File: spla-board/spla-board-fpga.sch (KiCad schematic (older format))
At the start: 32 parts, among them J2 J_JTAG, U1 LFE5U-45F-BG256

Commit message: schematic: Add Digikey and ManufacturerId fields to big components.
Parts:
- U1: Digikey (none) -> 220-2198-ND; Manufacturer Id (none) -> LFE4U-45F-6BG256C
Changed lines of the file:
@@
 F 2 "Package_BGA:BGA-256_14.0x14.0mm_Layout16x16_P0.8mm_Ball0.45mm_Pad0.32mm_NSMD" H 3050 4850 39  0001 C CNN
 F 3 "" H 3050 4850 39  0001 C CNN
+F 4 "220-2198-ND" H 4000 2850 50  0001 C CNN "Digikey"
+F 5 "LFE4U-45F-6BG256C" H 4000 2850 50  0001 C CNN "Manufacturer Id"
 	2    4000 2850
 	1    0    0    -1
@@
 F 2 "Package_BGA:BGA-256_14.0x14.0mm_Layout16x16_P0.8mm_Ball0.45mm_Pad0.32mm_NSMD" H 5550 4850 39  0001 C CNN
 F 3 "" H 5550 4850 39  0001 C CNN
+F 4 "220-2198-ND" H 6500 2850 50  0001 C CNN "Digikey"
+F 5 "LFE4U-45F-6BG256C" H 6500 2850 50  0001 C CNN "Manufacturer Id"
 	3    6500 2850
 	1    0    0    -1
@@
 F 2 "Package_BGA:BGA-256_14.0x14.0mm_Layout16x16_P0.8mm_Ball0.45mm_Pad0.32mm_NSMD" H 8050 4850 39  0001 C CNN
 F 3 "" H 8050 4850 39  0001 C CNN
+F 4 "220-2198-ND" H 9000 2850 50  0001 C CNN "Digikey"
+F 5 "LFE4U-45F-6BG256C" H 9000 2850 50  0001 C CNN "Manufacturer Id"
 	4    9000 2850
 	1    0    0    -1
@@
 F 2 "Package_BGA:BGA-256_14.0x14.0mm_Layout16x16_P0.8mm_Ball0.45mm_Pad0.32mm_NSMD" H 900 12100 39  0001 C CNN
 F 3 "" H 900 12100 39  0001 C CNN
+F 4 "220-2198-ND" H 1850 10100 50  0001 C CNN "Digikey"
+F 5 "LFE4U-45F-6BG256C" H 1850 10100 50  0001 C CNN "Manufacturer Id"
 	8    1850 10100
 	1    0    0    -1
@@
 F 2 "Package_BGA:BGA-256_14.0x14.0mm_Layout16x16_P0.8mm_Ball0.45mm_Pad0.32mm_NSMD" H 7900 12050 39  0001 C CNN
 F 3 "" H 7900 12050 39  0001 C CNN
+F 4 "220-2198-ND" H 8850 10050 50  0001 C CNN "Digikey"
+F 5 "LFE4U-45F-6BG256C" H 8850 10050 50  0001 C CNN "Manufacturer Id"
 	9    8850 10050
 	1    0    0    -1
@@
 F 2 "Package_BGA:BGA-256_14.0x14.0mm_Layout16x16_P0.8mm_Ball0.45mm_Pad0.32mm_NSMD" H 10550 4850 39  0001 C CNN
 F 3 "" H 10550 4850 39  0001 C CNN
+F 4 "220-2198-ND" H 11500 2850 50  0001 C CNN "Digikey"
+F 5 "LFE4U-45F-6BG256C" H 11500 2850 50  0001 C CNN "Manufacturer Id"
 	5    11500 2850
 	1    0    0    -1
@@
 F 2 "Package_BGA:BGA-256_14.0x14.0mm_Layout16x16_P0.8mm_Ball0.45mm_Pad0.32mm_NSMD" H 1500 9850 39  0001 C CNN
 F 3 "" H 1500 9850 39  0001 C CNN
+F 4 "220-2198-ND" H 2450 7850 50  0001 C CNN "Digikey"
+F 5 "LFE4U-45F-6BG256C" H 2450 7850 50  0001 C CNN "Manufacturer Id"
 	7    2450 7850
 	1    0    0    -1
@@
 F 2 "Package_BGA:BGA-256_14.0x14.0mm_Layout16x16_P0.8mm_Ball0.45mm_Pad0.32mm_NSMD" H 550 5250 39  0001 C CNN
 F 3 "" H 550 5250 39  0001 C CNN
+F 4 "220-2198-ND" H 1500 3250 50  0001 C CNN "Digikey"
+F 5 "LFE4U-45F-6BG256C" H 1500 3250 50  0001 C CNN "Manufacturer Id"
 	1    1500 3250
 	1    0    0    -1
@@
 F 2 "Package_BGA:BGA-256_14.0x14.0mm_Layout16x16_P0.8mm_Ball0.45mm_Pad0.32mm_NSMD" H 13050 4850 39  0001 C CNN
 F 3 "" H 13050 4850 39  0001 C CNN
+F 4 "220-2198-ND" H 14000 2850 50  0001 C CNN "Digikey"
+F 5 "LFE4U-45F-6BG256C" H 14000 2850 50  0001 C CNN "Manufacturer Id"
 	6    14000 2850
 	1    0    0    -1

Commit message: schematic: Select LED part.
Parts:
- D5, D6, D7, D8: Digikey (none) -> 732-4986-1-ND; Manufacturer Id (none) -> 150080VS75000
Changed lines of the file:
@@
 F 2 "LED_SMD:LED_0805_2012Metric" H 5550 9750 50  0001 C CNN
 F 3 "~" H 5550 9750 50  0001 C CNN
+F 4 "732-4986-1-ND" H 5550 9750 50  0001 C CNN "Digikey"
+F 5 "150080VS75000" H 5550 9750 50  0001 C CNN "Manufacturer Id"
 	1    5550 9750
 	0    -1   -1   0
@@
 F 2 "LED_SMD:LED_0805_2012Metric" H 5950 9750 50  0001 C CNN
 F 3 "~" H 5950 9750 50  0001 C CNN
+F 4 "732-4986-1-ND" H 5950 9750 50  0001 C CNN "Digikey"
+F 5 "150080VS75000" H 5950 9750 50  0001 C CNN "Manufacturer Id"
 	1    5950 9750
 	0    -1   -1   0
@@
 F 2 "LED_SMD:LED_0805_2012Metric" H 4750 9750 50  0001 C CNN
 F 3 "~" H 4750 9750 50  0001 C CNN
+F 4 "732-4986-1-ND" H 4750 9750 50  0001 C CNN "Digikey"
+F 5 "150080VS75000" H 4750 9750 50  0001 C CNN "Manufacturer Id"
 	1    4750 9750
 	0    -1   -1   0
@@
 F 2 "LED_SMD:LED_0805_2012Metric" H 5150 9750 50  0001 C CNN
 F 3 "~" H 5150 9750 50  0001 C CNN
+F 4 "732-4986-1-ND" H 5150 9750 50  0001 C CNN "Digikey"
+F 5 "150080VS75000" H 5150 9750 50  0001 C CNN "Manufacturer Id"
 	1    5150 9750
 	0    -1   -1   0

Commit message: schematic: Add part numbers for pinheaders (albeit that these are breakaways, and it's not one-per-part).
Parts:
- J2: Digikey (none) -> S1011EC-40-ND; Manufacturer Id (none) -> PRPC040SAAN-RC
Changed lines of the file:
@@
 F 2 "Connector_PinHeader_2.54mm:PinHeader_1x04_P2.54mm_Vertical" H 2700 9650 50  0001 C CNN
 F 3 "~" H 2700 9650 50  0001 C CNN
+F 4 "S1011EC-40-ND" H 2700 9650 50  0001 C CNN "Digikey"
+F 5 "PRPC040SAAN-RC" H 2700 9650 50  0001 C CNN "Manufacturer Id"
 	1    2700 9650
 	0    -1   -1   0

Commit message: schematic/pcb: Add test points for remaining three FPGA pins.
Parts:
- added TP7, TP8, TP9: TestPoint, TestPoint:TestPoint_Pad_D2.0mm, symbol Connector:TestPoint
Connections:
- net FPGA_EXTRA1: now reaches U1.C1 (PL14A)
- net FPGA_EXTRA1: now also TP7.1
- net FPGA_EXTRA2: now reaches U1.D1 (PL17A)
- net FPGA_EXTRA2: now also TP8.1
- net FPGA_EXTRA3: now reaches U1.E3 (PL14C)
- net FPGA_EXTRA3: now also TP9.1
- no-connect marks 21 -> 18
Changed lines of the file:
@@
 NoConn ~ 14650 3600
 NoConn ~ 14650 2500
-NoConn ~ 14650 1700
-NoConn ~ 14650 1900
-NoConn ~ 14650 2100
 NoConn ~ 7150 3600
 NoConn ~ 7150 3300
@@
 Text Notes 7950 7350 0    50   ~ 0
 Note: by above logic, 3.3V is short 9x 0.01uF decoupling capacitors, due to lack of space.
+Text GLabel 14650 1700 2    50   Output ~ 0
+FPGA_EXTRA1
+Text GLabel 14650 2100 2    50   Output ~ 0
+FPGA_EXTRA2
+Text GLabel 14650 1900 2    50   Output ~ 0
+FPGA_EXTRA3
+Text GLabel 14800 5300 2    50   Output ~ 0
+FPGA_EXTRA1
+Text GLabel 14800 5700 2    50   Output ~ 0
+FPGA_EXTRA2
+Text GLabel 14800 6100 2    50   Output ~ 0
+FPGA_EXTRA3
+$Comp
+L Connector:TestPoint TP7
+U 1 1 5EA65145
+P 14700 5200
+F 0 "TP7" H 14758 5318 50  0000 L CNN
+F 1 "TestPoint" H 14758 5227 50  0000 L CNN
+F 2 "TestPoint:TestPoint_Pad_D2.0mm" H 14900 5200 50  0001 C CNN
+F 3 "~" H 14900 5200 50  0001 C CNN
+	1    14700 5200
+	1    0    0    -1
+$EndComp
+$Comp
+L Connector:TestPoint TP8
+U 1 1 5EA6567A
+P 14700 5600
+F 0 "TP8" H 14758 5718 50  0000 L CNN
+F 1 "TestPoint" H 14758 5627 50  0000 L CNN
+F 2 "TestPoint:TestPoint_Pad_D2.0mm" H 14900 5600 50  0001 C CNN
+F 3 "~" H 14900 5600 50  0001 C CNN
+	1    14700 5600
+	1    0    0    -1
+$EndComp
+$Comp
+L Connector:TestPoint TP9
+U 1 1 5EA6C737
+P 14700 6000
+F 0 "TP9" H 14758 6118 50  0000 L CNN
+F 1 "TestPoint" H 14758 6027 50  0000 L CNN
+F 2 "TestPoint:TestPoint_Pad_D2.0mm" H 14900 6000 50  0001 C CNN
+F 3 "~" H 14900 6000 50  0001 C CNN
+	1    14700 6000
+	1    0    0    -1
+$EndComp
+Wire Wire Line
+	14800 5300 14700 5300
+Wire Wire Line
+	14700 5300 14700 5200
+Wire Wire Line
+	14800 5700 14700 5700
+Wire Wire Line
+	14700 5700 14700 5600
+Wire Wire Line
+	14800 6100 14700 6100
+Wire Wire Line
+	14700 6100 14700 6000
 $EndSCHEMATC

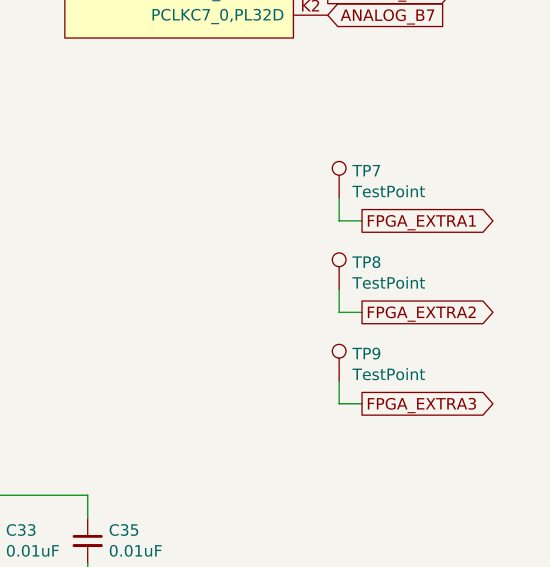
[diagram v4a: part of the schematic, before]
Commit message: schematic/pcb: Add BoM-only symbols.
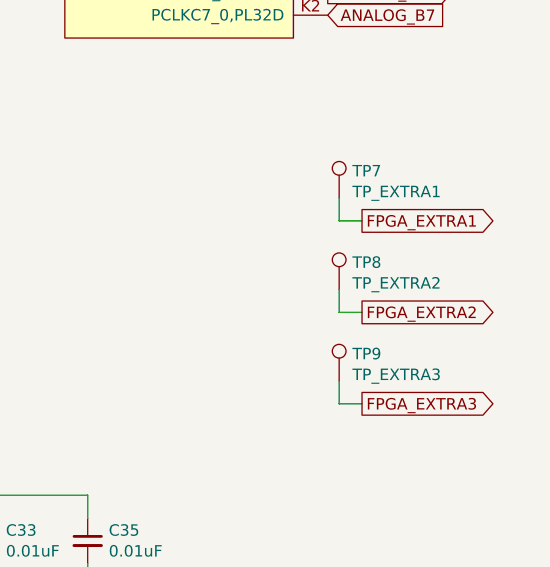
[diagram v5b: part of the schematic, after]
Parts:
- TP7: value TestPoint -> TP_EXTRA1; Digikey (none) -> N/A; Manufacturer Id (none) -> N/A
- TP8: value TestPoint -> TP_EXTRA2; Digikey (none) -> N/A; Manufacturer Id (none) -> N/A
- TP9: value TestPoint -> TP_EXTRA3; Digikey (none) -> N/A; Manufacturer Id (none) -> N/A
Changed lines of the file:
@@
 P 14700 5200
 F 0 "TP7" H 14758 5318 50  0000 L CNN
-F 1 "TestPoint" H 14758 5227 50  0000 L CNN
+F 1 "TP_EXTRA1" H 14758 5227 50  0000 L CNN
 F 2 "TestPoint:TestPoint_Pad_D2.0mm" H 14900 5200 50  0001 C CNN
 F 3 "~" H 14900 5200 50  0001 C CNN
+F 4 "N/A" H 14700 5200 50  0001 C CNN "Digikey"
+F 5 "N/A" H 14700 5200 50  0001 C CNN "Manufacturer Id"
 	1    14700 5200
 	1    0    0    -1
@@
 P 14700 5600
 F 0 "TP8" H 14758 5718 50  0000 L CNN
-F 1 "TestPoint" H 14758 5627 50  0000 L CNN
+F 1 "TP_EXTRA2" H 14758 5627 50  0000 L CNN
 F 2 "TestPoint:TestPoint_Pad_D2.0mm" H 14900 5600 50  0001 C CNN
 F 3 "~" H 14900 5600 50  0001 C CNN
+F 4 "N/A" H 14700 5600 50  0001 C CNN "Digikey"
+F 5 "N/A" H 14700 5600 50  0001 C CNN "Manufacturer Id"
 	1    14700 5600
 	1    0    0    -1
@@
 P 14700 6000
 F 0 "TP9" H 14758 6118 50  0000 L CNN
-F 1 "TestPoint" H 14758 6027 50  0000 L CNN
+F 1 "TP_EXTRA3" H 14758 6027 50  0000 L CNN
 F 2 "TestPoint:TestPoint_Pad_D2.0mm" H 14900 6000 50  0001 C CNN
 F 3 "~" H 14900 6000 50  0001 C CNN
+F 4 "N/A" H 14700 6000 50  0001 C CNN "Digikey"
+F 5 "N/A" H 14700 6000 50  0001 C CNN "Manufacturer Id"
 	1    14700 6000
 	1    0    0    -1

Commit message: bom: Add manufacturers.
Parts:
- D5, D6, D7, D8: Manufacturer (none) -> Wuerth Electronik
- J2: Manufacturer (none) -> Sullins Connector Solutions
- TP7, TP8, TP9: Manufacturer (none) -> N/A
- U1: Manufacturer (none) -> Lattice Semiconductor Corporation
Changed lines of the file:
@@
 F 4 "220-2198-ND" H 4000 2850 50  0001 C CNN "Digikey"
 F 5 "LFE4U-45F-6BG256C" H 4000 2850 50  0001 C CNN "Manufacturer Id"
+F 6 "Lattice Semiconductor Corporation" H 4000 2850 50  0001 C CNN "Manufacturer"
 	2    4000 2850
 	1    0    0    -1
@@
 F 4 "220-2198-ND" H 6500 2850 50  0001 C CNN "Digikey"
 F 5 "LFE4U-45F-6BG256C" H 6500 2850 50  0001 C CNN "Manufacturer Id"
+F 6 "Lattice Semiconductor Corporation" H 6500 2850 50  0001 C CNN "Manufacturer"
 	3    6500 2850
 	1    0    0    -1
@@
 F 4 "220-2198-ND" H 9000 2850 50  0001 C CNN "Digikey"
 F 5 "LFE4U-45F-6BG256C" H 9000 2850 50  0001 C CNN "Manufacturer Id"
+F 6 "Lattice Semiconductor Corporation" H 9000 2850 50  0001 C CNN "Manufacturer"
 	4    9000 2850
 	1    0    0    -1
@@
 F 4 "220-2198-ND" H 1850 10100 50  0001 C CNN "Digikey"
 F 5 "LFE4U-45F-6BG256C" H 1850 10100 50  0001 C CNN "Manufacturer Id"
+F 6 "Lattice Semiconductor Corporation" H 1850 10100 50  0001 C CNN "Manufacturer"
 	8    1850 10100
 	1    0    0    -1
@@
 F 4 "220-2198-ND" H 8850 10050 50  0001 C CNN "Digikey"
 F 5 "LFE4U-45F-6BG256C" H 8850 10050 50  0001 C CNN "Manufacturer Id"
+F 6 "Lattice Semiconductor Corporation" H 8850 10050 50  0001 C CNN "Manufacturer"
 	9    8850 10050
 	1    0    0    -1
@@
 F 4 "220-2198-ND" H 11500 2850 50  0001 C CNN "Digikey"
 F 5 "LFE4U-45F-6BG256C" H 11500 2850 50  0001 C CNN "Manufacturer Id"
+F 6 "Lattice Semiconductor Corporation" H 11500 2850 50  0001 C CNN "Manufacturer"
 	5    11500 2850
 	1    0    0    -1
@@
 F 4 "S1011EC-40-ND" H 2700 9650 50  0001 C CNN "Digikey"
 F 5 "PRPC040SAAN-RC" H 2700 9650 50  0001 C CNN "Manufacturer Id"
+F 6 "Sullins Connector Solutions" H 2700 9650 50  0001 C CNN "Manufacturer"
 	1    2700 9650
 	0    -1   -1   0
@@
 F 4 "220-2198-ND" H 2450 7850 50  0001 C CNN "Digikey"
 F 5 "LFE4U-45F-6BG256C" H 2450 7850 50  0001 C CNN "Manufacturer Id"
+F 6 "Lattice Semiconductor Corporation" H 2450 7850 50  0001 C CNN "Manufacturer"
 	7    2450 7850
 	1    0    0    -1
@@
 F 4 "220-2198-ND" H 1500 3250 50  0001 C CNN "Digikey"
 F 5 "LFE4U-45F-6BG256C" H 1500 3250 50  0001 C CNN "Manufacturer Id"
+F 6 "Lattice Semiconductor Corporation" H 1500 3250 50  0001 C CNN "Manufacturer"
 	1    1500 3250
 	1    0    0    -1
@@
 F 4 "220-2198-ND" H 14000 2850 50  0001 C CNN "Digikey"
 F 5 "LFE4U-45F-6BG256C" H 14000 2850 50  0001 C CNN "Manufacturer Id"
+F 6 "Lattice Semiconductor Corporation" H 14000 2850 50  0001 C CNN "Manufacturer"
 	6    14000 2850
 	1    0    0    -1
@@
 F 4 "732-4986-1-ND" H 5550 9750 50  0001 C CNN "Digikey"
 F 5 "150080VS75000" H 5550 9750 50  0001 C CNN "Manufacturer Id"
+F 6 "Wuerth Electronik" H 5550 9750 50  0001 C CNN "Manufacturer"
 	1    5550 9750
 	0    -1   -1   0
@@
 F 4 "732-4986-1-ND" H 5950 9750 50  0001 C CNN "Digikey"
 F 5 "150080VS75000" H 5950 9750 50  0001 C CNN "Manufacturer Id"
+F 6 "Wuerth Electronik" H 5950 9750 50  0001 C CNN "Manufacturer"
 	1    5950 9750
 	0    -1   -1   0
@@
 F 4 "732-4986-1-ND" H 4750 9750 50  0001 C CNN "Digikey"
 F 5 "150080VS75000" H 4750 9750 50  0001 C CNN "Manufacturer Id"
+F 6 "Wuerth Electronik" H 4750 9750 50  0001 C CNN "Manufacturer"
 	1    4750 9750
 	0    -1   -1   0
@@
 F 4 "732-4986-1-ND" H 5150 9750 50  0001 C CNN "Digikey"
 F 5 "150080VS75000" H 5150 9750 50  0001 C CNN "Manufacturer Id"
+F 6 "Wuerth Electronik" H 5150 9750 50  0001 C CNN "Manufacturer"
 	1    5150 9750
 	0    -1   -1   0
@@
 F 4 "N/A" H 14700 5200 50  0001 C CNN "Digikey"
 F 5 "N/A" H 14700 5200 50  0001 C CNN "Manufacturer Id"
+F 6 "N/A" H 14700 5200 50  0001 C CNN "Manufacturer"
 	1    14700 5200
 	1    0    0    -1
@@
 F 4 "N/A" H 14700 5600 50  0001 C CNN "Digikey"
 F 5 "N/A" H 14700 5600 50  0001 C CNN "Manufacturer Id"
+F 6 "N/A" H 14700 5600 50  0001 C CNN "Manufacturer"
 	1    14700 5600
 	1    0    0    -1
@@
 F 4 "N/A" H 14700 6000 50  0001 C CNN "Digikey"
 F 5 "N/A" H 14700 6000 50  0001 C CNN "Manufacturer Id"
+F 6 "N/A" H 14700 6000 50  0001 C CNN "Manufacturer"
 	1    14700 6000
 	1    0    0    -1
